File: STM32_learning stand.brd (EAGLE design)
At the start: 100 x 90 mm, 131 parts, among them J1 Power in, J10 RS-485_1, J11 RS-485_2, J12 FD CAN 1, J13 FD CAN 2, J15 Motor, J2 ST-link, J3 Encoder, J4 BMS_interface, J5 S6B-PH-K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

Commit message: small update
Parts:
- moved U4 0.25 mm to (59.2, 57.2)

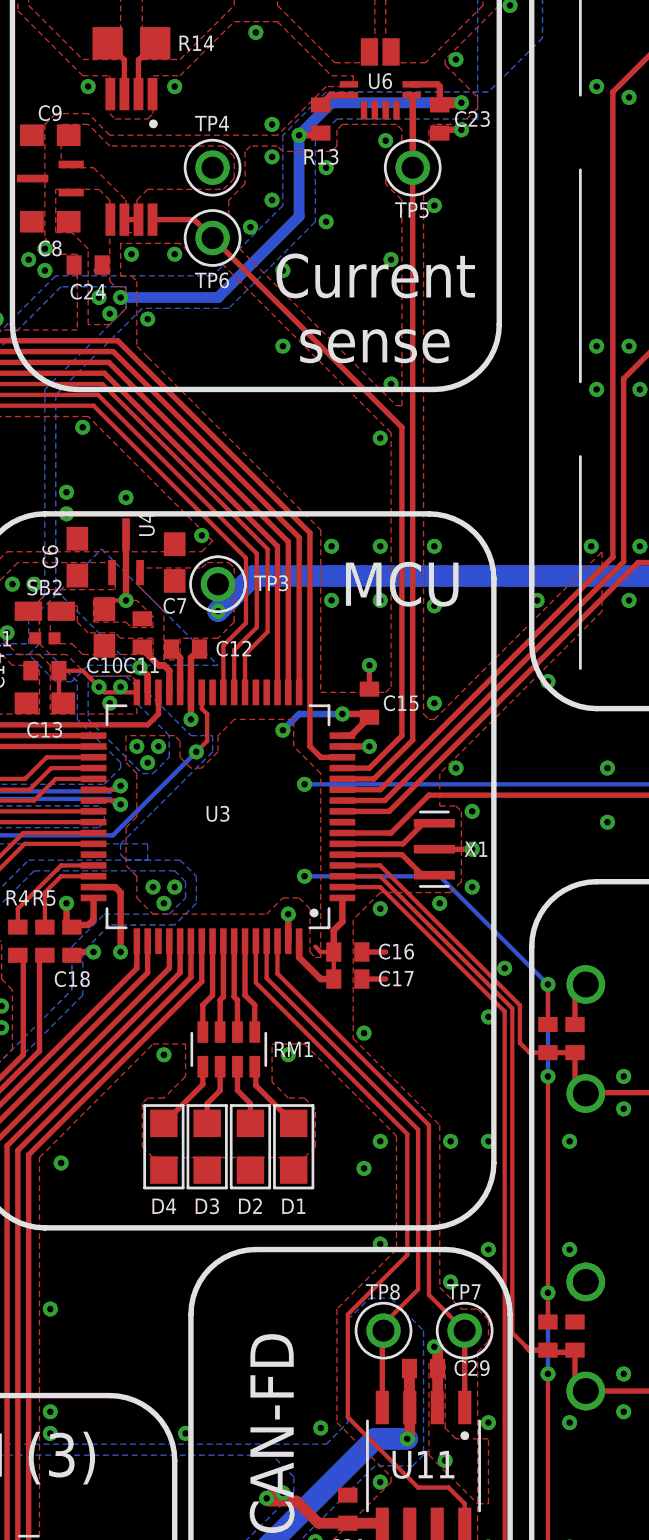
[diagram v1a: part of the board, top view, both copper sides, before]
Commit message: Added calibration and better current measurement organiztion
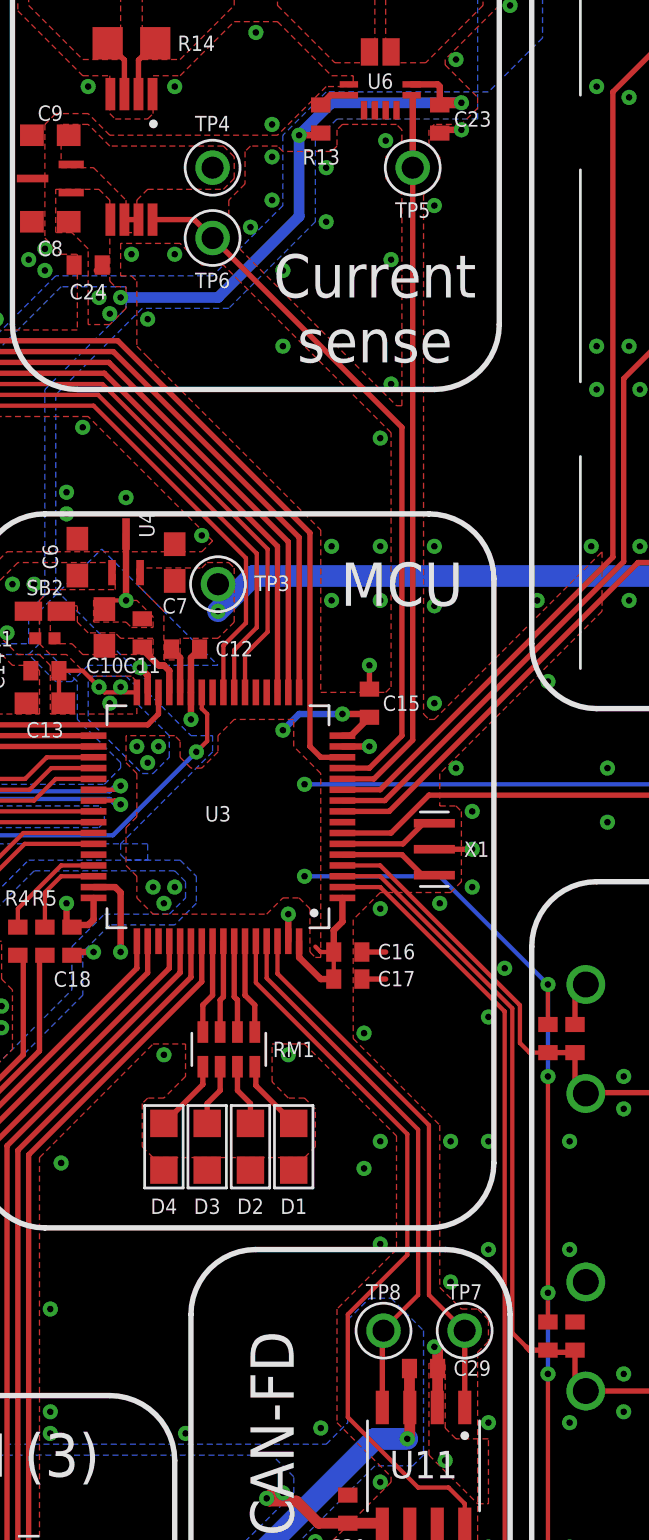
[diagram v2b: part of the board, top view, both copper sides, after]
